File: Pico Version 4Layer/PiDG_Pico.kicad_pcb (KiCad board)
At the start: 4 copper layers, 126 x 126 mm, 84 parts, among them J1 Conn_02x05_Odd_Even, J10 Trig, J11 Laser Enable, J12 Pixel Reset, J14 Pico Socket A, J15 Pico Socket B, J16 Laser En/PWM Trig/GND, J17 USB-C PD in, J18 Laser 1 mode, J19 Laser 2 mode, J2 Conn_02x05_Odd_Even, J3 Conn_02x05_Odd_Even, J4 Conn_02x05_Odd_Even, J5 Conn_02x05_Odd_Even, J6 Conn_02x05_Odd_Even, J7 Laser 1, J8 Laser 2, U1 74LVC1G04, U10 74AHCT1G08, U12 74LVC1G17, U13 UCC27524, U14 CH224A, U15 AP63205WU, U16 LM66100, U17 LT3065EDD, U18 TPS3700DDC, U2 SN74LVC04AD, U3 74LVC1G00, U4 SN74LVC04AD, U5 74LVC1G04, U6 SN74LVC04AD, U7 74AHCT1G08, U8 74AHCT1G08, U9 NCP718xSN180

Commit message: JLC cost-down and laser amplitude margin for the Pico board
Availability and cost (JLC data of 2026-10-05):
- U9: NCP718BSN180T1G (C892792), in stock; NCP718ASN180T1G has none.
  Same datasheet, pinout and +/-2 % 1.8 V output. Pre-order: 162 pcs.
- R25/R26: Yageo AC2512FK-7W47RL (C7209419), higher stock.
- U18 divider R21/R22/R23 -> 150k / 1.2k / 4.7k, all JLC basic parts
  (removes two extended lines).

Laser amplitude margin:
- U13 (UCC27524, SOIC-8 D package) has ROH 5 typ / 8.5 max ohm with no
  minimum (SLUSFA9), not the 2.5-7.5 ohm used before. With 101k the 50 ohm
  high corner reached 5.19 V (0.3 % below the 5.2 V limit).
- R12 101k -> 100k 0.1 % (C122537): +12V is 11.8 V (11.54-12.05 V), and the
  50 ohm output is 4.54-5.14 V (0.8 % / 1.2 % margin). Hi-Z mode 4.55-5.08 V.
- U18 retuned for the new rail: UV 10.6 V rising (release <= 10.89 V,
  0.65 V below the rail band), OV 13.3 V (12.88-13.67 V, 0.82 V above it).
- The DSD package (ROH 2.5-7.5 ohm) was rejected: 25 ns max minimum pulse
  width and 4 ns channel matching break the 20 ns WIDTH and 1-2 ns matching.

Docs, BOMs, CPL, README and schematic notes updated. ERC/DRC: no new
findings against the previous commit; gerbers unchanged.

Co-Authored-By: Claude Opus 5.5 <noreply@anthropic.com>
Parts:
- R12: value 101k -> 100k
- R21: value 1M -> 150k
- R22: value 6.04k -> 1.2k
- R23: value 31.6k -> 4.7k
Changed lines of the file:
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@@
 			)
 		)
-		(property "Value" "1M"
+		(property "Value" "150k"
 			(at 0 1.65 90)
 			(layer "F.Fab")
@@
 			)
 		)
-		(property "Description" "TPS3700 window divider top (1 %)"
+		(property "Description" "TPS3700 window divider top (1 %): 150k"
 			(at 0 0 90)
 			(layer "F.Fab")
@@
 			)
 		)
-		(property "Value" "101k"
+		(property "Value" "100k"
 			(at 0 1.65 0)
 			(layer "F.Fab")
@@
 			)
 		)
-		(property "Description" "LT3065 feedback top, 0.1 % thin film: 11.906 V = 0.6 V x (1 + 101k/5.36k)"
+		(property "Description" "LT3065 feedback top, 0.1 % thin film: 11.794 V = 0.6 V x (1 + 100k/5.36k)"
 			(at 0 0 0)
 			(layer "F.Fab")
@@
 			)
 		)
-		(property "Value" "6.04k"
+		(property "Value" "1.2k"
 			(at 0 1.65 90)
 			(layer "F.Fab")
@@
 			)
 		)
-		(property "Description" "TPS3700 window divider middle (1 %): UV 11.0 V rising / 10.9 V falling"
+		(property "Description" "TPS3700 window divider middle (1 %): UV 10.6 V rising / 10.4 V falling"
 			(at 0 0 90)
 			(layer "F.Fab")
@@
 			)
 		)
-		(property "Description" "Series resistor, 2 W 2512. 50 ohm mode (J18 on 1-2): 11.9 V x 50/(50+68+ROH) = 4.61-5.08 V into the 50 ohm LDP-V trigger input"
+		(property "Description" "Series resistor, 2 W 2512. 50 ohm mode (J18 on 1-2): 11.8 V x 50/(50+68+ROH) = 4.54-5.14 V into the 50 ohm LDP-V trigger input (ROH 0-8.5 ohm)"
 			(at 0 0 0)
 			(layer "F.Fab")
@@
 			)
 		)
-		(property "Description" "Laser power-good: OUTA low if +12V < 11.0 V (UV), OUTB low if +12V > 13.1 V (OV). Drives U13 ENA/ENB."
+		(property "Description" "Laser power-good: OUTA low if +12V < 10.6 V (UV), OUTB low if +12V > 13.3 V (OV). Drives U13 ENA/ENB."
 			(at 0 0 90)
 			(layer "F.Fab")
@@
 			)
 		)
-		(property "Description" "12 V laser rail: 45 V / 500 mA LDO. VOUT = 0.6 V x (1 + R12/R13) = 11.9 V. R20 sets a 400 mA current limit."
+		(property "Description" "12 V laser rail: 45 V / 500 mA LDO. VOUT = 0.6 V x (1 + R12/R13) = 11.8 V. R20 sets a 400 mA current limit."
 			(at 0 0 90)
 			(layer "F.Fab")
@@
 			)
 		)
-		(property "Description" "Series resistor, 2 W 2512. 50 ohm mode (J19 on 1-2): 11.9 V x 50/(50+68+ROH) = 4.61-5.08 V into the 50 ohm LDP-V trigger input"
+		(property "Description" "Series resistor, 2 W 2512. 50 ohm mode (J19 on 1-2): 11.8 V x 50/(50+68+ROH) = 4.54-5.14 V into the 50 ohm LDP-V trigger input (ROH 0-8.5 ohm)"
 			(at 0 0 0)
 			(layer "F.Fab")
@@
 			)
 		)
-		(property "Value" "31.6k"
+		(property "Value" "4.7k"
 			(at 0 1.65 90)
 			(layer "F.Fab")
@@
 			)
 		)
-		(property "Description" "TPS3700 window divider bottom (1 %): OV 13.1 V rising"
+		(property "Description" "TPS3700 window divider bottom (1 %): OV 13.3 V rising"
 			(at 0 0 90)
 			(layer "F.Fab")

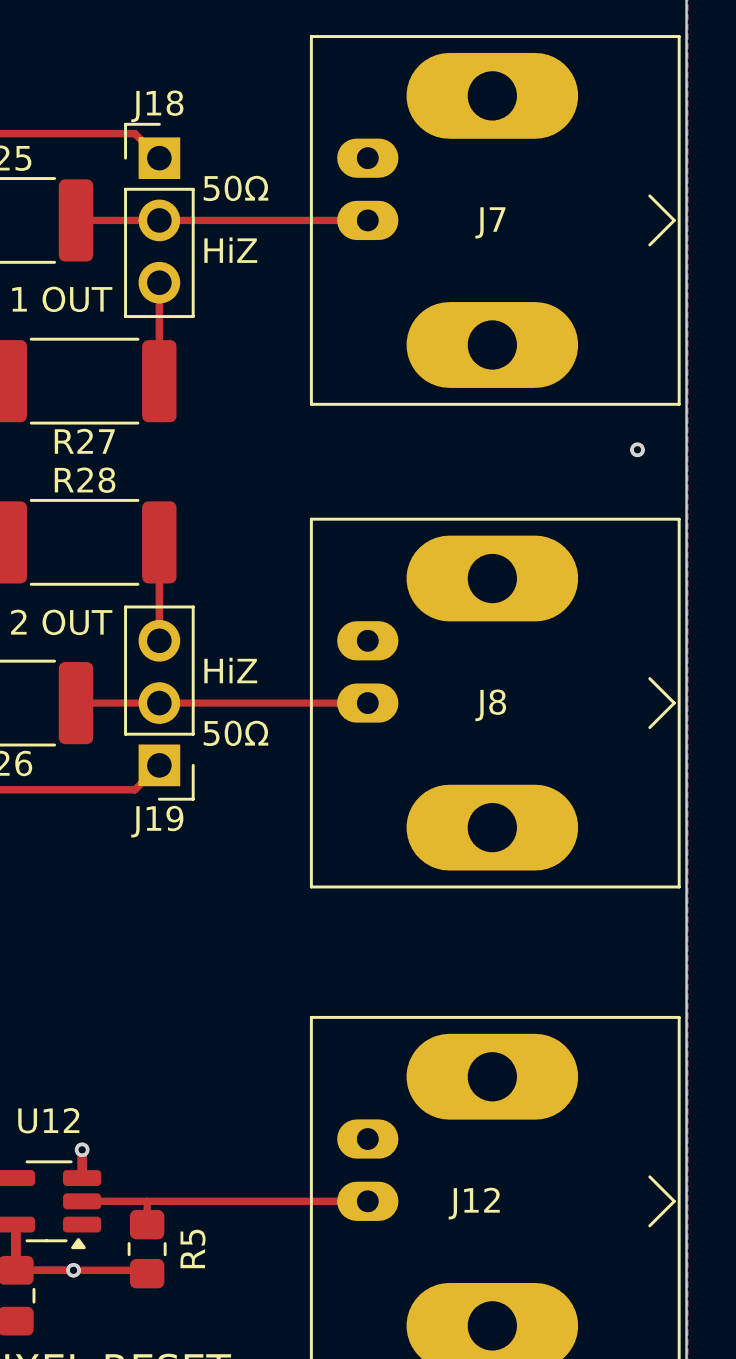
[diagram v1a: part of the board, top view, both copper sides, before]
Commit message: Pico BNCs: Kinghelm KH-BNC50-3511 as the default part
- J7/J8/J12: Kinghelm KH-BNC50-3511 (C2837587, ~$0.93) replaces the
  Amphenol B6252HB-NPP3G-50 (C22457552, ~$3.61). 50 ohm only; never the
  KH-BNC75-3511. Saves about $34 per 5-board order.
- New footprint PiDG_Local:BNC_Kinghelm_KH-BNC50-3511_Horizontal, made
  from the board instance: Amphenol pad pattern (Kinghelm drawing matches
  within 0.04 mm), pin holes 0.89 -> 0.90 mm (Kinghelm recommended size),
  post holes 2.01 mm unchanged. 3D model is still the Amphenol body.
- Schematic and board fields (footprint, datasheet, description), BOMs,
  CPL, fp-lib-table description, Hardware.md and JLC_ORDER.md updated:
  test-fit two parts and check shell-to-GND continuity before release;
  tip ~20.6 mm past the edge, axis ~6.6 mm up (measure on first board).
- Zones refilled; gerbers, drill files and gerber zip regenerated.
  DRC/ERC: no new findings against the previous commit.

Co-Authored-By: Claude Opus 5.5 <noreply@anthropic.com>
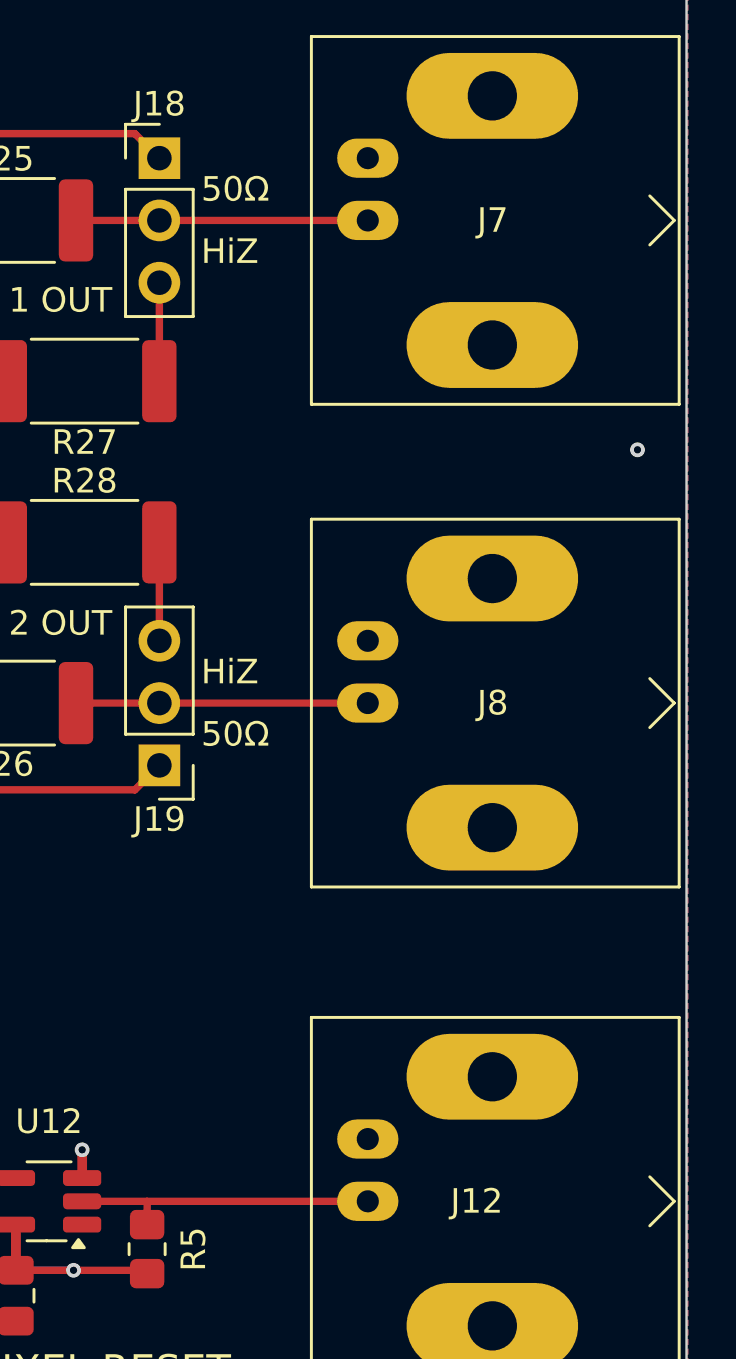
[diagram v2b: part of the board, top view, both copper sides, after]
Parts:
- J12, J7, J8: footprint Connector_Coaxial:BNC_Amphenol_B6252HB-NPP3G-50_Horizontal -> PiDG_Local:BNC_Kinghelm_KH-BNC50-3511_Horizontal
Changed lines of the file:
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@@
 		)
 	)
-	(footprint "Connector_Coaxial:BNC_Amphenol_B6252HB-NPP3G-50_Horizontal"
+	(footprint "PiDG_Local:BNC_Kinghelm_KH-BNC50-3511_Horizontal"
 		(layer "F.Cu")
 		(at 245 100.33 -90)
@@
 			)
 		)
-		(property "Datasheet" "~"
+		(property "Datasheet" "https://wmsc.lcsc.com/wmsc/upload/file/pdf/v2/lcsc/2211231430_Shenzhen-Kinghelm-Elec-KH-BNC50-3511_C2837587.pdf"
 			(at 0 0 270)
 			(unlocked yes)
@@
 			)
 		)
-		(property "Description" "coaxial connector (BNC, SMA, SMB, SMC, Cinch/RCA, LEMO, ...)"
+		(property "Description" "BNC 50 ohm right-angle jack, Kinghelm KH-BNC50-3511 (LCSC C2837587). Never the 75 ohm KH-BNC75-3511."
 			(at 0 0 270)
 			(unlocked yes)
@@
 			(at 0 0 270)
 			(size 1.6 2.5)
-			(drill 0.89)
+			(drill 0.9)
 			(layers "*.Cu" "*.Mask")
 			(remove_unused_layers no)
@@
 			(at -2.54 0 270)
 			(size 1.6 2.5)
-			(drill 0.89)
+			(drill 0.9)
 			(layers "*.Cu" "*.Mask")
 			(remove_unused_layers no)
@@
 		)
 	)
-	(footprint "Connector_Coaxial:BNC_Amphenol_B6252HB-NPP3G-50_Horizontal"
+	(footprint "PiDG_Local:BNC_Kinghelm_KH-BNC50-3511_Horizontal"
 		(layer "F.Cu")
 		(at 245 120.65 -90)
@@
 			)
 		)
-		(property "Datasheet" "~"
+		(property "Datasheet" "https://wmsc.lcsc.com/wmsc/upload/file/pdf/v2/lcsc/2211231430_Shenzhen-Kinghelm-Elec-KH-BNC50-3511_C2837587.pdf"
 			(at 0 0 270)
 			(unlocked yes)
@@
 			)
 		)
-		(property "Description" "coaxial connector (BNC, SMA, SMB, SMC, Cinch/RCA, LEMO, ...)"
+		(property "Description" "BNC 50 ohm right-angle jack, Kinghelm KH-BNC50-3511 (LCSC C2837587). Never the 75 ohm KH-BNC75-3511."
 			(at 0 0 270)
 			(unlocked yes)
@@
 			(at 0 0 270)
 			(size 1.6 2.5)
-			(drill 0.89)
+			(drill 0.9)
 			(layers "*.Cu" "*.Mask")
 			(remove_unused_layers no)
@@
 			(at -2.54 0 270)
 			(size 1.6 2.5)
-			(drill 0.89)
+			(drill 0.9)
 			(layers "*.Cu" "*.Mask")
 			(remove_unused_layers no)
@@
 		)
 	)
-	(footprint "Connector_Coaxial:BNC_Amphenol_B6252HB-NPP3G-50_Horizontal"
+	(footprint "PiDG_Local:BNC_Kinghelm_KH-BNC50-3511_Horizontal"
 		(layer "F.Cu")
 		(at 245 80.645 -90)
@@
 			)
 		)
-		(property "Datasheet" "~"
+		(property "Datasheet" "https://wmsc.lcsc.com/wmsc/upload/file/pdf/v2/lcsc/2211231430_Shenzhen-Kinghelm-Elec-KH-BNC50-3511_C2837587.pdf"
 			(at 0 0 270)
 			(unlocked yes)
@@
 			)
 		)
-		(property "Description" "coaxial connector (BNC, SMA, SMB, SMC, Cinch/RCA, LEMO, ...)"
+		(property "Description" "BNC 50 ohm right-angle jack, Kinghelm KH-BNC50-3511 (LCSC C2837587). Never the 75 ohm KH-BNC75-3511."
 			(at 0 0 270)
 			(unlocked yes)
@@
 			(at 0 0 270)
 			(size 1.6 2.5)
-			(drill 0.89)
+			(drill 0.9)
 			(layers "*.Cu" "*.Mask")
 			(remove_unused_layers no)
@@
 			(at -2.54 0 270)
 			(size 1.6 2.5)
-			(drill 0.89)
+			(drill 0.9)
 			(layers "*.Cu" "*.Mask")
 			(remove_unused_layers no)
